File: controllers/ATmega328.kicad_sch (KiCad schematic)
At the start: 10 parts, among them U401 ATMEGA328P-AU, Y407 8MHz

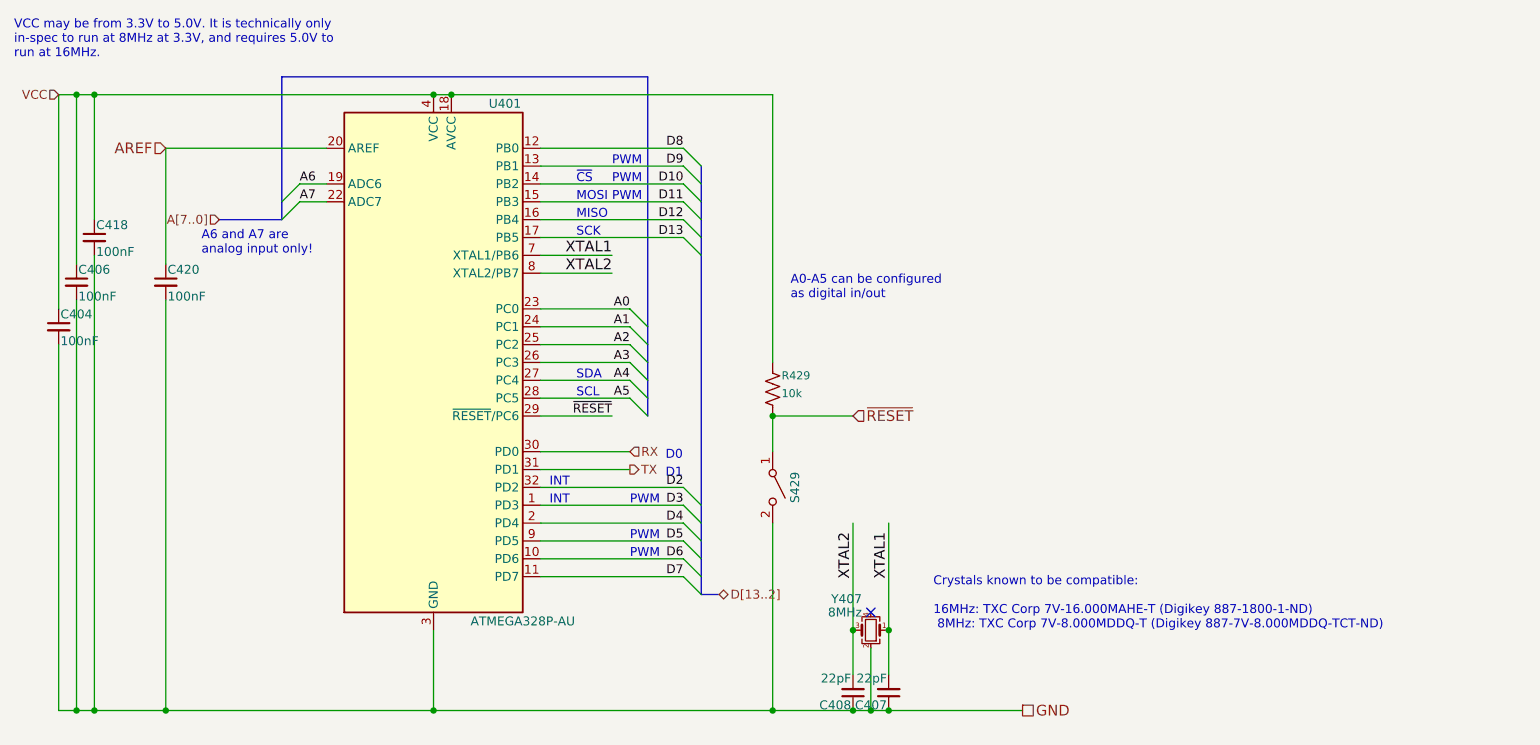
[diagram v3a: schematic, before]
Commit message: Add text references Cx20 etc to support re-numbering the components when imporing into a different project.
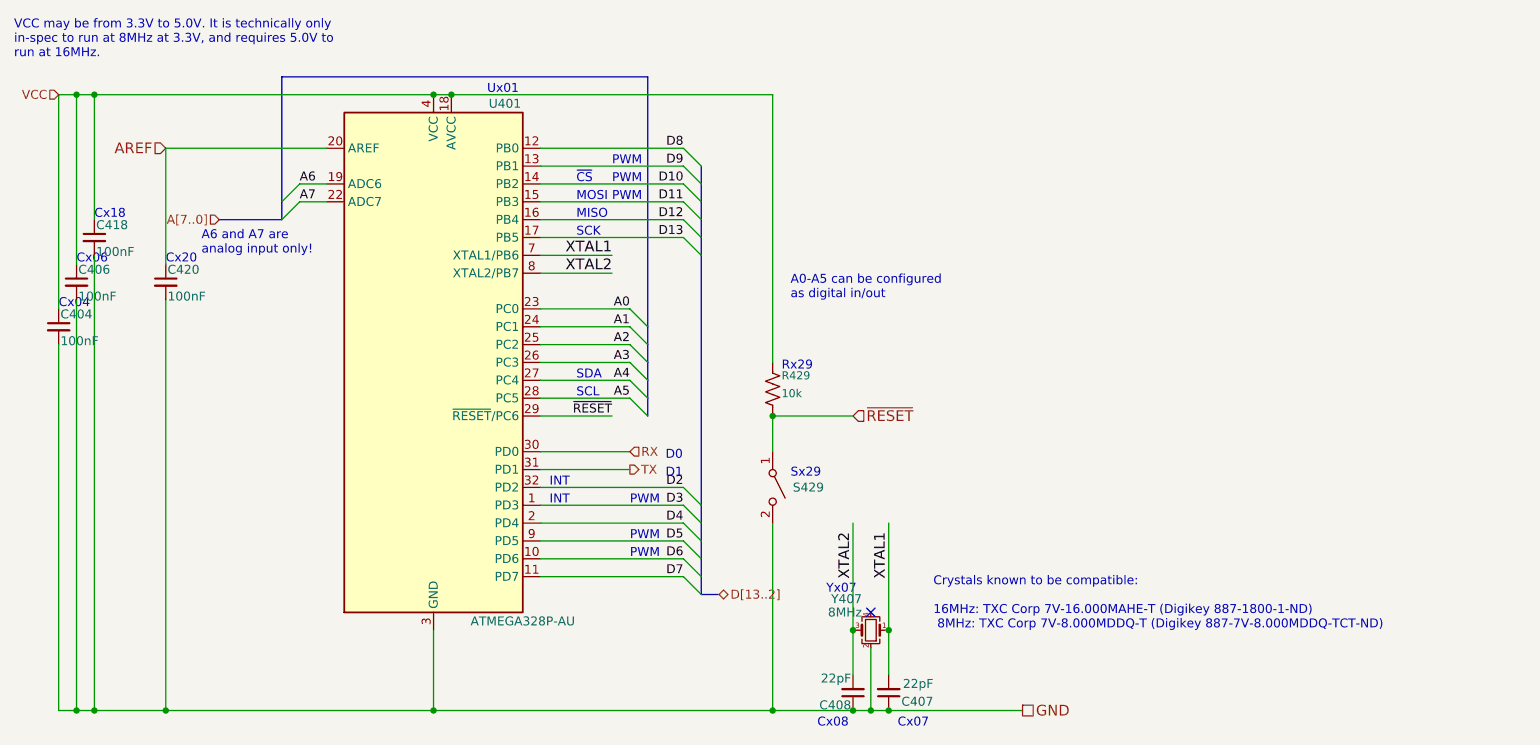
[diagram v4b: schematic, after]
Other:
- note added: "Cx04"
- note added: "Cx06"
- note added: "Cx07"
- note added: "Cx08"
- note added: "Cx18"
- note added: "Cx20"
- note added: "Rx29"
- note added: "Sx29"
- note added: "Ux01"
- note added: "Yx07"
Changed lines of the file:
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@@
+    (effects (font (size 1.27 1.27)) (justify left bottom))
+  )
+  (text "Cx06" (at 25.4 49.53 0)
     (effects (font (size 1.27 1.27)) (justify left bottom))
   )
@@
     (effects (font (size 1.27 1.27)) (justify left bottom))
   )
+  (text "Cx04" (at 22.86 55.88 0)
+    (effects (font (size 1.27 1.27)) (justify left bottom))
+  )
   (text "PWM" (at 101.6 40.64 0)
     (effects (font (size 1.27 1.27)) (justify left bottom))
@@
   )
   (text "INT" (at 92.71 81.28 0)
+    (effects (font (size 1.27 1.27)) (justify left bottom))
+  )
+  (text "Cx08" (at 130.81 115.57 0)
+    (effects (font (size 1.27 1.27)) (justify left bottom))
+  )
+  (text "Sx29" (at 127 80.01 0)
+    (effects (font (size 1.27 1.27)) (justify left bottom))
+  )
+  (text "Cx07" (at 142.24 115.57 0)
+    (effects (font (size 1.27 1.27)) (justify left bottom))
+  )
+  (text "Yx07" (at 132.08 96.52 0)
     (effects (font (size 1.27 1.27)) (justify left bottom))
   )
@@
     (effects (font (size 1.27 1.27)) (justify left bottom))
   )
+  (text "Cx18" (at 27.94 43.18 0)
+    (effects (font (size 1.27 1.27)) (justify left bottom))
+  )
   (text "PWM" (at 101.6 38.1 0)
     (effects (font (size 1.27 1.27)) (justify left bottom))
@@
     (effects (font (size 1.27 1.27)) (justify left bottom))
   )
+  (text "Cx20" (at 38.1 49.53 0)
+    (effects (font (size 1.27 1.27)) (justify left bottom))
+  )
   (text "PWM" (at 104.14 83.82 0)
     (effects (font (size 1.27 1.27)) (justify left bottom))
   )
+  (text "Rx29" (at 125.73 64.77 0)
+    (effects (font (size 1.27 1.27)) (justify left bottom))
+  )
   (text "PWM" (at 101.6 35.56 0)
+    (effects (font (size 1.27 1.27)) (justify left bottom))
+  )
+  (text "Ux01" (at 83.82 25.4 0)
     (effects (font (size 1.27 1.27)) (justify left bottom))
   )
@@
       )
       (project "Precision23"
-        (path "/9151f981-b383-4946-8df4-92ef46ef2206/9f66be35-2744-413f-8b31-a996047a434b/84662bc9-aa4f-4f0d-8756-174283206cf9"
+        (path "/9151f981-b383-4946-8df4-92ef46ef2206/b9b5a9b9-9a45-4bb4-8a5d-f3809553447a/9407dcb2-4240-4949-9fc7-e511c818f8d4"
           (reference "C420") (unit 1)
         )
@@
       )
       (project "Precision23"
-        (path "/9151f981-b383-4946-8df4-92ef46ef2206/9f66be35-2744-413f-8b31-a996047a434b/84662bc9-aa4f-4f0d-8756-174283206cf9"
+        (path "/9151f981-b383-4946-8df4-92ef46ef2206/b9b5a9b9-9a45-4bb4-8a5d-f3809553447a/9407dcb2-4240-4949-9fc7-e511c818f8d4"
           (reference "C418") (unit 1)
         )
@@
       )
       (project "Precision23"
-        (path "/9151f981-b383-4946-8df4-92ef46ef2206/9f66be35-2744-413f-8b31-a996047a434b/84662bc9-aa4f-4f0d-8756-174283206cf9"
+        (path "/9151f981-b383-4946-8df4-92ef46ef2206/b9b5a9b9-9a45-4bb4-8a5d-f3809553447a/9407dcb2-4240-4949-9fc7-e511c818f8d4"
           (reference "C406") (unit 1)
         )
@@
       )
       (project "Precision23"
-        (path "/9151f981-b383-4946-8df4-92ef46ef2206/9f66be35-2744-413f-8b31-a996047a434b/84662bc9-aa4f-4f0d-8756-174283206cf9"
+        (path "/9151f981-b383-4946-8df4-92ef46ef2206/b9b5a9b9-9a45-4bb4-8a5d-f3809553447a/9407dcb2-4240-4949-9fc7-e511c818f8d4"
           (reference "C404") (unit 1)
         )
@@
       )
       (project "Precision23"
-        (path "/9151f981-b383-4946-8df4-92ef46ef2206/9f66be35-2744-413f-8b31-a996047a434b/84662bc9-aa4f-4f0d-8756-174283206cf9"
+        (path "/9151f981-b383-4946-8df4-92ef46ef2206/b9b5a9b9-9a45-4bb4-8a5d-f3809553447a/9407dcb2-4240-4949-9fc7-e511c818f8d4"
           (reference "Y407") (unit 1)
         )
@@
   (symbol (lib_id "Device:C_Small") (at 140.97 110.49 180) (unit 1)
     (in_bom yes) (on_board yes) (dnp no)
-    (property "Reference" "C407" (at 140.716 112.268 0)
-      (effects (font (size 1.27 1.27)) (justify left))
-    )
-    (property "Value" "22pF" (at 140.716 108.458 0)
+    (property "Reference" "C407" (at 147.32 111.76 0)
+      (effects (font (size 1.27 1.27)) (justify left))
+    )
+    (property "Value" "22pF" (at 147.32 109.22 0)
       (effects (font (size 1.27 1.27)) (justify left))
     )
@@
       )
       (project "Precision23"
-        (path "/9151f981-b383-4946-8df4-92ef46ef2206/9f66be35-2744-413f-8b31-a996047a434b/84662bc9-aa4f-4f0d-8756-174283206cf9"
+        (path "/9151f981-b383-4946-8df4-92ef46ef2206/b9b5a9b9-9a45-4bb4-8a5d-f3809553447a/9407dcb2-4240-4949-9fc7-e511c818f8d4"
           (reference "C407") (unit 1)
         )
@@
       )
       (project "Precision23"
-        (path "/9151f981-b383-4946-8df4-92ef46ef2206/9f66be35-2744-413f-8b31-a996047a434b/84662bc9-aa4f-4f0d-8756-174283206cf9"
+        (path "/9151f981-b383-4946-8df4-92ef46ef2206/b9b5a9b9-9a45-4bb4-8a5d-f3809553447a/9407dcb2-4240-4949-9fc7-e511c818f8d4"
           (reference "C408") (unit 1)
         )
@@
   (symbol (lib_id "Switch:SW_SPST") (at 124.46 81.28 270) (unit 1)
     (in_bom yes) (on_board yes) (dnp no)
-    (property "Reference" "S429" (at 127.635 81.28 0)
+    (property "Reference" "S429" (at 129.54 81.28 90)
       (effects (font (size 1.27 1.27)))
     )
@@
       )
       (project "Precision23"
-        (path "/9151f981-b383-4946-8df4-92ef46ef2206/9f66be35-2744-413f-8b31-a996047a434b/84662bc9-aa4f-4f0d-8756-174283206cf9"
+        (path "/9151f981-b383-4946-8df4-92ef46ef2206/b9b5a9b9-9a45-4bb4-8a5d-f3809553447a/9407dcb2-4240-4949-9fc7-e511c818f8d4"
           (reference "S429") (unit 1)
         )
@@
       )
       (project "Precision23"
-        (path "/9151f981-b383-4946-8df4-92ef46ef2206/9f66be35-2744-413f-8b31-a996047a434b/84662bc9-aa4f-4f0d-8756-174283206cf9"
+        (path "/9151f981-b383-4946-8df4-92ef46ef2206/b9b5a9b9-9a45-4bb4-8a5d-f3809553447a/9407dcb2-4240-4949-9fc7-e511c818f8d4"
           (reference "R429") (unit 1)
         )
@@
       )
       (project "Precision23"
-        (path "/9151f981-b383-4946-8df4-92ef46ef2206/9f66be35-2744-413f-8b31-a996047a434b/84662bc9-aa4f-4f0d-8756-174283206cf9"
+        (path "/9151f981-b383-4946-8df4-92ef46ef2206/b9b5a9b9-9a45-4bb4-8a5d-f3809553447a/9407dcb2-4240-4949-9fc7-e511c818f8d4"
           (reference "U401") (unit 1)
         )
